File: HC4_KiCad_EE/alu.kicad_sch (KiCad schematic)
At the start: 8 parts, among them IC3 74HC253, IC4 74HC253, IC7 74HC283

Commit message: 仕様決め
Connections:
- net ALU_OUT0: now also IC3.6 (I0a)
- net ALU_OUT1: now also IC3.10 (I0b)
- net ALU_OUT2: now also IC4.6 (I0a)
- net ALU_OUT3: now also IC4.10 (I0b)
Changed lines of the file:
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@@
+	(wire
+		(pts
+			(xy 190.5 33.02) (xy 200.66 33.02)
+		)
+		(stroke
+			(width 0)
+			(type default)
+		)
+	)
 	(wire
 		(pts
@@
 	(wire
 		(pts
+			(xy 200.66 58.42) (xy 190.5 58.42)
+		)
+		(stroke
+			(width 0)
+			(type default)
+		)
+	)
+	(wire
+		(pts
+			(xy 200.66 115.57) (xy 190.5 115.57)
+		)
+		(stroke
+			(width 0)
+			(type default)
+		)
+	)
+	(wire
+		(pts
+			(xy 190.5 92.71) (xy 200.66 92.71)
+		)
+		(stroke
+			(width 0)
+			(type default)
+		)
+	)
+	(wire
+		(pts
 			(xy 163.83 60.96) (xy 172.72 60.96)
 		)
@@
 	(wire
 		(pts
+			(xy 200.66 35.56) (xy 190.5 35.56)
+		)
+		(stroke
+			(width 0)
+			(type default)
+		)
+	)
+	(wire
+		(pts
 			(xy 128.27 63.5) (xy 138.43 63.5)
 		)
@@
 		)
 	)
+	(wire
+		(pts
+			(xy 200.66 118.11) (xy 190.5 118.11)
+		)
+		(stroke
+			(width 0)
+			(type default)
+		)
+	)
 	(bus
 		(pts
@@
 	(wire
 		(pts
+			(xy 190.5 50.8) (xy 200.66 50.8)
+		)
+		(stroke
+			(width 0)
+			(type default)
+		)
+	)
+	(wire
+		(pts
+			(xy 200.66 55.88) (xy 190.5 55.88)
+		)
+		(stroke
+			(width 0)
+			(type default)
+		)
+	)
+	(wire
+		(pts
 			(xy 128.27 73.66) (xy 138.43 73.66)
 		)
@@
 		)
 	)
+	(wire
+		(pts
+			(xy 200.66 53.34) (xy 190.5 53.34)
+		)
+		(stroke
+			(width 0)
+			(type default)
+		)
+	)
 	(bus
 		(pts
@@
 	(wire
 		(pts
+			(xy 200.66 113.03) (xy 190.5 113.03)
+		)
+		(stroke
+			(width 0)
+			(type default)
+		)
+	)
+	(wire
+		(pts
 			(xy 128.27 60.96) (xy 138.43 60.96)
 		)
@@
 	(wire
 		(pts
+			(xy 200.66 100.33) (xy 190.5 100.33)
+		)
+		(stroke
+			(width 0)
+			(type default)
+		)
+	)
+	(wire
+		(pts
 			(xy 128.27 78.74) (xy 138.43 78.74)
 		)
@@
 	(wire
 		(pts
+			(xy 200.66 38.1) (xy 190.5 38.1)
+		)
+		(stroke
+			(width 0)
+			(type default)
+		)
+	)
+	(wire
+		(pts
 			(xy 88.9 167.64) (xy 101.6 167.64)
 		)
@@
 	(wire
 		(pts
+			(xy 200.66 40.64) (xy 190.5 40.64)
+		)
+		(stroke
+			(width 0)
+			(type default)
+		)
+	)
+	(wire
+		(pts
 			(xy 163.83 53.34) (xy 172.72 53.34)
 		)
@@
 	(wire
 		(pts
+			(xy 200.66 97.79) (xy 190.5 97.79)
+		)
+		(stroke
+			(width 0)
+			(type default)
+		)
+	)
+	(wire
+		(pts
 			(xy 63.5 175.26) (xy 76.2 175.26)
 		)
@@
 		)
 		(stroke
+			(width 0)
+			(type default)
+		)
+	)
+	(wire
+		(pts
+			(xy 190.5 110.49) (xy 200.66 110.49)
+		)
+		(stroke
+			(width 0)
+			(type default)
+		)
+	)
+	(wire
+		(pts
+			(xy 200.66 95.25) (xy 190.5 95.25)
+		)
+		(stroke

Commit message: コミット忘れてたてへ
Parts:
- added IC6: 74HC86, symbol 74xx_2:74HC86
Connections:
- net ALU_in_A0: now also IC6.1
- net ALU_in_A1: now also IC6.4
- net ALU_in_A2: now also IC6.9
- net ALU_in_A3: now also IC6.12
- net ALU_in_B0: now also IC6.2
- net ALU_in_B1: now also IC6.5
- net ALU_in_B2: now also IC6.10
- net ALU_in_B3: now also IC6.13
- net GND: now also IC7.8 (GND)
- net VCC: now also IC7.16 (VCC)
- net ADDER3: now reaches IC4.11 (I1b)
- net ADDER3: now also IC7.10 (S4)
- net ADDER2: now reaches IC4.5 (I1a)
- net ADDER2: now also IC7.13 (S3)
- net ADDER1: now reaches IC3.11 (I1b)
- net ADDER1: now also IC7.1 (S2)
- net ADDER0: now reaches IC3.5 (I1a)
- net ADDER0: now also IC7.4 (S1)
- net ALU_OUT0: no longer names the net of IC3.6 (I0a)
- net ALU_OUT0: no longer IC7.4 (S1)
- net ALU_OUT1: no longer names the net of IC3.10 (I0b)
- net ALU_OUT1: no longer IC7.1 (S2)
- net ALU_OUT2: no longer names the net of IC4.6 (I0a)
- net ALU_OUT2: no longer IC7.13 (S3)
- net ALU_OUT3: no longer names the net of IC4.10 (I0b)
- net ALU_OUT3: no longer IC7.10 (S4)

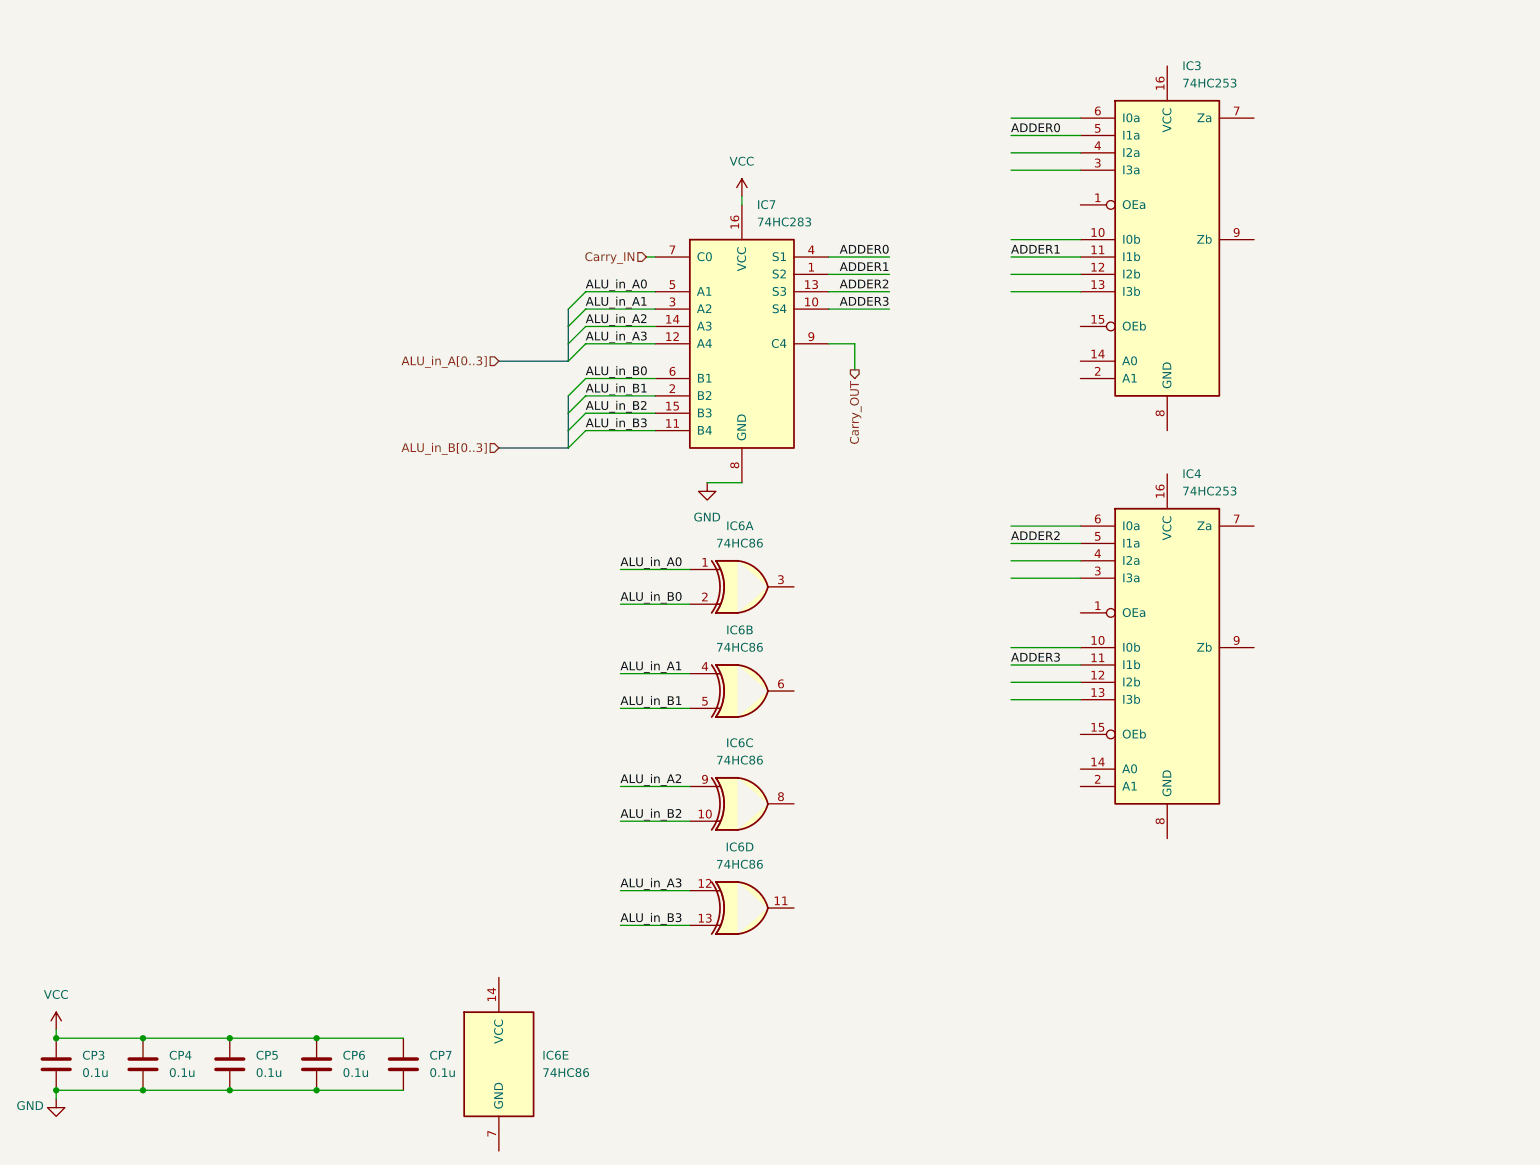
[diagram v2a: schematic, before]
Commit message: 4809を別シートに、ほか
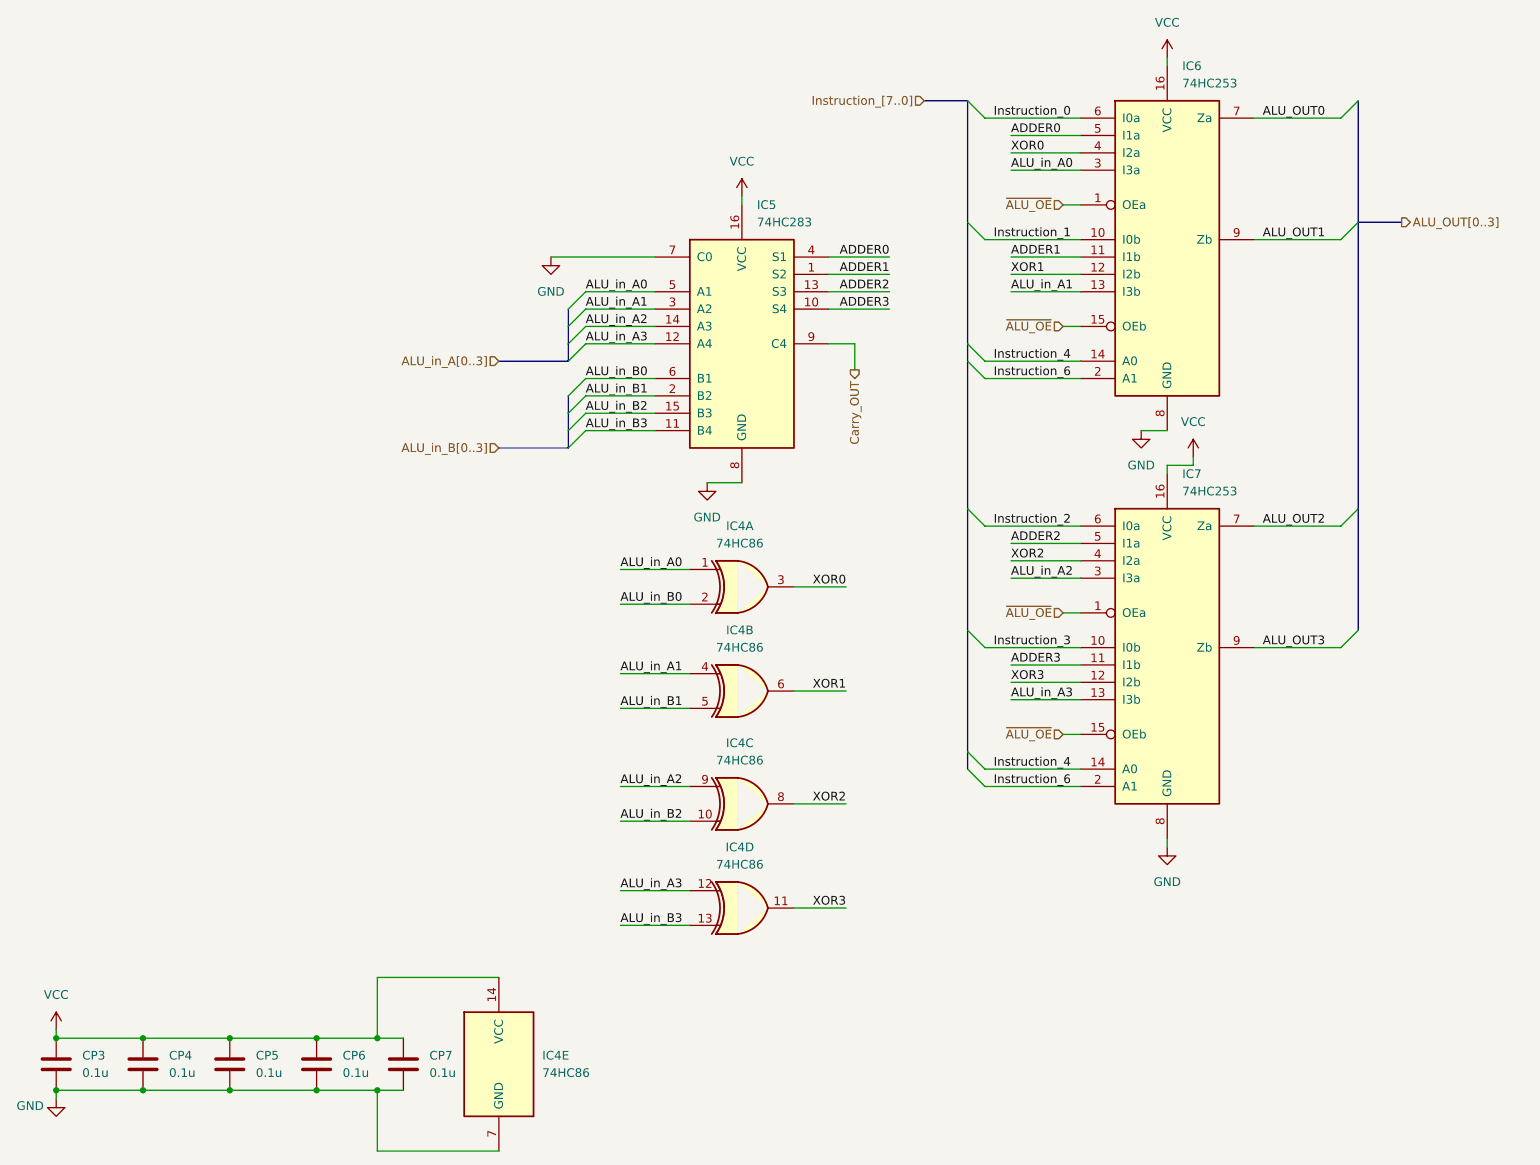
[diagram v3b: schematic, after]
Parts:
- renumbered IC6 to IC4, IC7 to IC5, IC3 to IC6, IC4 to IC7
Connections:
- net Carry_IN is gone; now on net GND: IC5.7 (C0)
- net ALU_in_A0: now also IC6.3 (I3a)
- net ALU_in_A1: now also IC6.13 (I3b)
- net ALU_in_A2: now also IC7.3 (I3a)
- net ALU_in_A3: now also IC7.13 (I3b)
- net GND: now also IC4.7 (GND), IC6.8 (GND), IC7.8 (GND)
- net VCC: now also IC4.14 (VCC), IC6.16 (VCC), IC7.16 (VCC)
- net XOR0: now reaches IC4.3
- net XOR0: now also IC6.4 (I2a)
- net XOR1: now reaches IC4.6
- net XOR1: now also IC6.12 (I2b)
- net XOR2: now reaches IC4.8
- net XOR2: now also IC7.4 (I2a)
- net ~{ALU_OE}: now reaches IC7.1 (OEa)
- net ~{ALU_OE}: now also IC6.1 (OEa), IC6.15 (OEb), IC7.15 (OEb)
- net Instruction_3: now reaches IC7.10 (I0b)
- net XOR3: now reaches IC7.12 (I2b)
- net XOR3: now also IC4.11
- net Instruction_4: now reaches IC7.14 (A0)
- net Instruction_4: now also IC6.14 (A0)
- net Instruction_6: now reaches IC7.2 (A1)
- net Instruction_6: now also IC6.2 (A1)
- net Instruction_2: now reaches IC7.6 (I0a)
- net ALU_OUT2: now reaches IC7.7 (Za)
- net ALU_OUT3: now reaches IC7.9 (Zb)
- net Instruction_1: now reaches IC6.10 (I0b)
- net Instruction_0: now reaches IC6.6 (I0a)
- net ALU_OUT0: now reaches IC6.7 (Za)
- net ALU_OUT1: now reaches IC6.9 (Zb)

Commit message: 完成かも～
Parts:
- removed CP7: 0.1u, Capacitor_THT:C_Disc_D3.0mm_W1.6mm_P2.50mm, symbol Device2:C_Bypass
- renumbered IC4 to IC1, IC5 to IC2, IC6 to IC3, IC7 to IC4
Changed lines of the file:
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@@
 	)
 	(junction
-		(at 97.79 167.64)
-		(diameter 0)
-		(color 0 0 0 0)
-	)
-	(junction
 		(at 50.8 167.64)
 		(diameter 0)
@@
 	)
 	(junction
-		(at 97.79 175.26)
-		(diameter 0)
-		(color 0 0 0 0)
-	)
-	(junction
 		(at 88.9 175.26)
 		(diameter 0)
@@
 	(wire
 		(pts
-			(xy 97.79 175.26) (xy 101.6 175.26)
-		)
-		(stroke
-			(width 0)
-			(type default)
-		)
-	)
-	(wire
-		(pts
 			(xy 63.5 175.26) (xy 76.2 175.26)
 		)
@@
 	(wire
 		(pts
-			(xy 97.79 167.64) (xy 101.6 167.64)
-		)
-		(stroke
-			(width 0)
-			(type default)
-		)
-	)
-	(wire
-		(pts
 			(xy 128.27 66.04) (xy 138.43 66.04)
 		)
@@
 		(dnp no)
 		(fields_autoplaced yes)
-		(property "Reference" "#PWR013"
+		(property "Reference" "#PWR011"
 			(at 151.13 48.26 0)
 			(effects
@@
 			(project ""
 				(path "/33731ded-38c0-4297-bdd8-92b082f46ff8/51fb15b9-2319-4d69-a07a-a04158a23ae2"
-					(reference "#PWR013")
+					(reference "#PWR011")
 					(unit 1)
 				)
@@
 		(dnp no)
 		(fields_autoplaced yes)
-		(property "Reference" "IC4"
+		(property "Reference" "IC1"
 			(at 150.8252 92.71 0)
 			(effects
@@
 			(project ""
 				(path "/33731ded-38c0-4297-bdd8-92b082f46ff8/51fb15b9-2319-4d69-a07a-a04158a23ae2"
-					(reference "IC4")
+					(reference "IC1")
 					(unit 1)
 				)
@@
 		(dnp no)
 		(fields_autoplaced yes)
-		(property "Reference" "IC4"
+		(property "Reference" "IC1"
 			(at 150.8252 107.95 0)
 			(effects
@@
 			(project ""
 				(path "/33731ded-38c0-4297-bdd8-92b082f46ff8/51fb15b9-2319-4d69-a07a-a04158a23ae2"
-					(reference "IC4")
+					(reference "IC1")
 					(unit 2)
 				)
@@
 		(dnp no)
 		(fields_autoplaced yes)
-		(property "Reference" "IC4"
+		(property "Reference" "IC1"
 			(at 150.8252 124.46 0)
 			(effects
@@
 			(project ""
 				(path "/33731ded-38c0-4297-bdd8-92b082f46ff8/51fb15b9-2319-4d69-a07a-a04158a23ae2"
-					(reference "IC4")
+					(reference "IC1")
 					(unit 3)
 				)
@@
 		(dnp no)
 		(fields_autoplaced yes)
-		(property "Reference" "IC4"
+		(property "Reference" "IC1"
 			(at 121.92 170.1799 0)
 			(effects
@@
 			(project ""
 				(path "/33731ded-38c0-4297-bdd8-92b082f46ff8/51fb15b9-2319-4d69-a07a-a04158a23ae2"
-					(reference "IC4")
+					(reference "IC1")
 					(unit 5)
 				)
@@
 		(dnp no)
 		(fields_autoplaced yes)
-		(property "Reference" "#PWR010"
+		(property "Reference" "#PWR07"
 			(at 50.8 170.18 0)
 			(effects
@@
 			(project "HC4_KiCad"
 				(path "/33731ded-38c0-4297-bdd8-92b082f46ff8/51fb15b9-2319-4d69-a07a-a04158a23ae2"
-					(reference "#PWR010")
+					(reference "#PWR07")
 					(unit 1)
 				)
@@
 		(dnp no)
 		(fields_autoplaced yes)
-		(property "Reference" "#PWR055"
+		(property "Reference" "#PWR014"
 			(at 213.36 146.05 0)
 			(effects
@@
 			(project "HC4_KiCad_EE"
 				(path "/33731ded-38c0-4297-bdd8-92b082f46ff8/51fb15b9-2319-4d69-a07a-a04158a23ae2"
-					(reference "#PWR055")
+					(reference "#PWR014")
 					(unit 1)
 				)
@@
 		(dnp no)
 		(fields_autoplaced yes)
-		(property "Reference" "#PWR054"
+		(property "Reference" "#PWR09"
 			(at 123.19 59.69 0)
 			(effects
@@
 			(project ""
 				(path "/33731ded-38c0-4297-bdd8-92b082f46ff8/51fb15b9-2319-4d69-a07a-a04158a23ae2"
-					(reference "#PWR054")
+					(reference "#PWR09")
 					(unit 1)
 				)
@@
 		(on_board yes)
 		(dnp no)
-		(property "Reference" "#PWR011"
+		(property "Reference" "#PWR08"
 			(at 50.8 182.88 0)
 			(effects
@@
 			(project "HC4_KiCad"
 				(path "/33731ded-38c0-4297-bdd8-92b082f46ff8/51fb15b9-2319-4d69-a07a-a04158a23ae2"
-					(reference "#PWR011")
+					(reference "#PWR08")
 					(unit 1)
 				)
@@
 		(dnp no)
 		(fields_autoplaced yes)
-		(property "Reference" "#PWR08"
+		(property "Reference" "#PWR015"
 			(at 217.17 86.36 0)
 			(effects
@@
 			(project ""
 				(path "/33731ded-38c0-4297-bdd8-92b082f46ff8/51fb15b9-2319-4d69-a07a-a04158a23ae2"
-					(reference "#PWR08")
+					(reference "#PWR015")
 					(unit 1)
 				)
@@
 		(dnp no)
 		(fields_autoplaced yes)
-		(property "Reference" "IC7"
+		(property "Reference" "IC4"
 			(at 215.5541 85.09 0)
 			(effects
@@
 			(project "HC4_KiCad_EE"
 				(path "/33731ded-38c0-4297-bdd8-92b082f46ff8/51fb15b9-2319-4d69-a07a-a04158a23ae2"
-					(reference "IC7")
+					(reference "IC4")
 					(unit 1)
 				)
@@
 		(dnp no)
 		(fields_autoplaced yes)
-		(property "Reference" "#PWR07"
+		(property "Reference" "#PWR012"
 			(at 209.55 85.09 0)
 			(effects
@@
 			(project ""
 				(path "/33731ded-38c0-4297-bdd8-92b082f46ff8/51fb15b9-2319-4d69-a07a-a04158a23ae2"
-					(reference "#PWR07")
+					(reference "#PWR012")
 					(unit 1)
 				)
@@
 		(dnp no)
 		(fields_autoplaced yes)
-		(property "Reference" "IC4"
+		(property "Reference" "IC1"
 			(at 150.8252 139.7 0)
 			(effects
@@
 			(project ""
 				(path "/33731ded-38c0-4297-bdd8-92b082f46ff8/51fb15b9-2319-4d69-a07a-a04158a23ae2"
-					(reference "IC4")
+					(reference "IC1")
 					(unit 4)
 				)
@@
 		(dnp no)
 		(fields_autoplaced yes)
-		(property "Reference" "IC5"
+		(property "Reference" "IC2"
 			(at 153.3241 45.72 0)
 			(effects
@@
 			(project ""
 				(path "/33731ded-38c0-4297-bdd8-92b082f46ff8/51fb15b9-2319-4d69-a07a-a04158a23ae2"
-					(reference "IC5")
-					(unit 1)
-				)
-			)
-		)
-	)
-	(symbol
-		(lib_id "Device2:C_Bypass")
-		(at 101.6 171.45 0)
-		(unit 1)
-		(exclude_from_sim no)
-		(in_bom yes)
-		(on_board yes)
-		(dnp no)
-		(fields_autoplaced yes)
-		(property "Reference" "CP7"
-			(at 105.41 170.1799 0)
-			(effects
-				(font
-					(size 1.27 1.27)
-				)
-				(justify left)
-			)
-		)
-		(property "Value" "0.1u"
-			(at 105.41 172.7199 0)
-			(effects
-				(font
-					(size 1.27 1.27)
-				)
-				(justify left)
-			)
-		)
-		(property "Footprint" "Capacitor_THT:C_Disc_D3.0mm_W1.6mm_P2.50mm"
-			(at 102.5652 175.26 0)
-			(effects
-				(font
-					(size 1.27 1.27)
-				)
-				(hide yes)
-			)
-		)
-		(property "Datasheet" "~"
-			(at 101.6 171.45 0)
-			(effects
-				(font
-					(size 1.27 1.27)
-				)
-				(hide yes)
-			)
-		)
-		(property "Description" "Bypass Capacitor"
-			(at 101.6 171.45 0)
-			(effects
-				(font
-					(size 1.27 1.27)
-				)
-				(hide yes)
-			)
-		)
-		(pin "2"
-		)
-		(pin "1"
-		)
-		(instances
-			(project "HC4_KiCad"
-				(path "/33731ded-38c0-4297-bdd8-92b082f46ff8/51fb15b9-2319-4d69-a07a-a04158a23ae2"
-					(reference "CP7")
+					(reference "IC2")
 					(unit 1)
 				)
@@
 		(dnp no)
 		(fields_autoplaced yes)
-		(property "Reference" "#PWR056"
+		(property "Reference" "#PWR013"
 			(at 213.36 27.94 0)
 			(effects
@@
 			(project "HC4_KiCad_EE"
 				(path "/33731ded-38c0-4297-bdd8-92b082f46ff8/51fb15b9-2319-4d69-a07a-a04158a23ae2"
-					(reference "#PWR056")
+					(reference "#PWR013")
 					(unit 1)
 				)
@@
 		(dnp no)
 		(fields_autoplaced yes)
-		(property "Reference" "#PWR012"
+		(property "Reference" "#PWR010"
 			(at 146.05 92.71 0)
 			(effects
@@
 			(project ""
 				(path "/33731ded-38c0-4297-bdd8-92b082f46ff8/51fb15b9-2319-4d69-a07a-a04158a23ae2"
-					(reference "#PWR012")
+					(reference "#PWR010")
 					(unit 1)
 				)
@@
 		(dnp no)
 		(fields_autoplaced yes)
-		(property "Reference" "IC6"
+		(property "Reference" "IC3"
 			(at 215.5541 25.4 0)
 			(effects
@@
 			(project ""
 				(path "/33731ded-38c0-4297-bdd8-92b082f46ff8/51fb15b9-2319-4d69-a07a-a04158a23ae2"
-					(reference "IC6")
+					(reference "IC3")
 					(unit 1)
 				)

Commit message: Carry_ENを論理反転、回路図の修正
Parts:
- renumbered CP3 to CP1, CP4 to CP2, CP5 to CP3, CP6 to CP4
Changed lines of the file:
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@@
 		(dnp no)
 		(fields_autoplaced yes)
-		(property "Reference" "CP5"
+		(property "Reference" "CP3"
 			(at 80.01 170.1799 0)
 			(effects
@@
 			(project "HC4_KiCad"
 				(path "/33731ded-38c0-4297-bdd8-92b082f46ff8/51fb15b9-2319-4d69-a07a-a04158a23ae2"
-					(reference "CP5")
+					(reference "CP3")
 					(unit 1)
 				)
@@
 		(dnp no)
 		(fields_autoplaced yes)
-		(property "Reference" "CP6"
+		(property "Reference" "CP4"
 			(at 92.71 170.1799 0)
 			(effects
@@
 			(project "HC4_KiCad"
 				(path "/33731ded-38c0-4297-bdd8-92b082f46ff8/51fb15b9-2319-4d69-a07a-a04158a23ae2"
-					(reference "CP6")
+					(reference "CP4")
 					(unit 1)
 				)
@@
 		(dnp no)
 		(fields_autoplaced yes)
-		(property "Reference" "CP3"
+		(property "Reference" "CP1"
 			(at 54.61 170.1799 0)
 			(effects
@@
 			(project ""
 				(path "/33731ded-38c0-4297-bdd8-92b082f46ff8/51fb15b9-2319-4d69-a07a-a04158a23ae2"
-					(reference "CP3")
+					(reference "CP1")
 					(unit 1)
 				)
@@
 		(dnp no)
 		(fields_autoplaced yes)
-		(property "Reference" "CP4"
+		(property "Reference" "CP2"
 			(at 67.31 170.1799 0)
 			(effects
@@
 			(project "HC4_KiCad"
 				(path "/33731ded-38c0-4297-bdd8-92b082f46ff8/51fb15b9-2319-4d69-a07a-a04158a23ae2"
-					(reference "CP4")
+					(reference "CP2")
 					(unit 1)
 				)
